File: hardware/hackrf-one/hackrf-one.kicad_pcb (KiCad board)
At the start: 4 copper layers, 120 x 75 mm, 431 parts, among them J1 USB-MICRO-B, J10 GND_CLIP, J2 RF-SHIELD-FRAME, J3 RF-SHIELD-COVER, J4 MOUNTING_HOLE, J5 MOUNTING_HOLE, J6 MOUNTING_HOLE, J7 MOUNTING_HOLE, J8 MOUNTING_HOLE, J9 MOUNTING_HOLE, P13 GPO1, P14 XCVR_CLKOUT, P15 INTR, P16 CLKIN, P17 GPO6, P18 OEB, P19 GPO3, P2 CLKOUT, P20 GPIO, P21 REF_IN, P22 I2S, P23 DBGEN, P24 TRST, P25 LPC_ISP, P26 LPC_JTAG, P27 MIXER_SDATA, P28 SD, P29 CPLD_JTAG, P3 GND, P30 BANK2_AUX, P31 MIXER_SCLK, P32 MIXER_ENX, P33 MIXER_RESETX, P34 MIX_BYPASS, P35 !MIX_BYPASS, P37 SCL, P38 SDA, P39 SSP1_SCK, P4 ANTENNA, P40 SSP1_COPI, P41 SSP1_CIPO, P43 RX, P44 HP, P45 LP, P46 TX_MIX_BP, P47 RX_MIX_BP, P48 TX_AMP, P49 RX_AMP, P5 LEDS, P50 AMP_BYPASS, P51 !TX_AMP_PWR, P52 !RX_AMP_PWR, P53 CS_XCVR, P54 CS_AD, P55 TXENABLE, P56 RXENABLE, P57 XTAL2, P58 GCK1, P59 GCK2, P6 GPO4, P60 SGPIO_CLK, P61 DA0, P62 DA7, P63 DD0, P64 DD9, P65 DA4, P66 DD5, P67 RSSI, P68 SPIFI_CS, P69 VREGMODE, P7 GPO2, P70 EN_1V8, P71 ID, P72 GP_CLKIN, P73 P1_2, P74 P1_1, P75 GP_CLKIN, P76 GP_CLKIN, P77 GP_CLKIN, P78 GP_CLKIN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

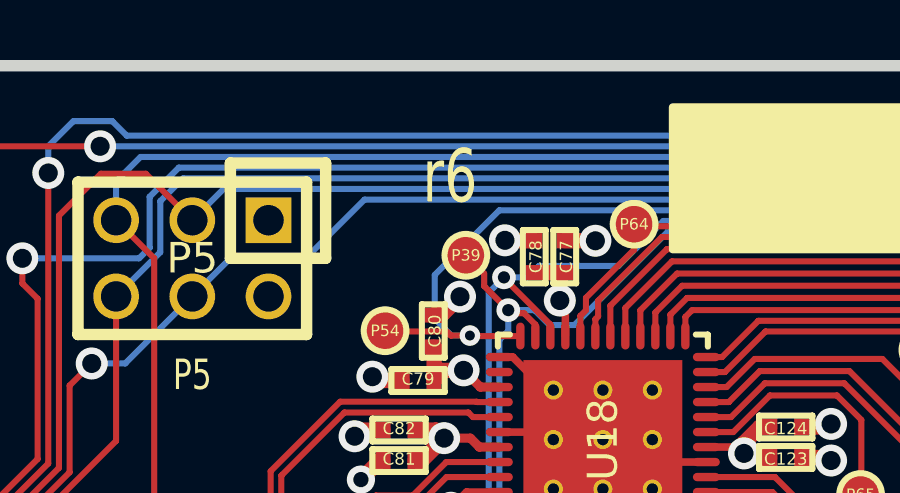
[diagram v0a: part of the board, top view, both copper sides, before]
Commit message: HackRF One: Change all references from r6 to r8
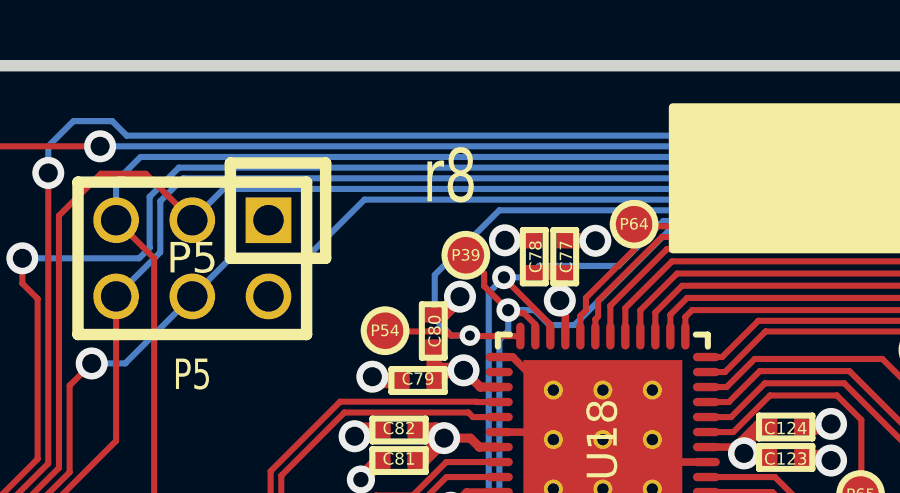
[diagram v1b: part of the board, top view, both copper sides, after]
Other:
- board text added: "r8"
- board text removed: "r6"
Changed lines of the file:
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@@
     (title "HackRF One")
     (date 2020-07-21)
-    (rev r6)
+    (rev r8)
     (company "Copyright 2012-2020 Great Scott Gadgets")
     (comment 1 "Michael Ossmann")
@@
       (net 192 GND))
   )
-  (gr_text r6 (at 97.8 103.7) (layer F.SilkS)
+  (gr_text r8 (at 97.8 103.7) (layer F.SilkS)
     (effects (font (size 1.778 1.27) (thickness 0.3048)))
   )

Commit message: HackRF One: update VBUS sense resistor values
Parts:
- R62: value 0 -> 10k
- R65: value 10k -> 18k
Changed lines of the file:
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@@
       (effects (font (size 0.4064 0.4064) (thickness 0.1016)))
     )
-    (fp_text value 0 (at 0 0.0508) (layer F.SilkS) hide
+    (fp_text value 10k (at 0 0.0508) (layer F.SilkS) hide
       (effects (font (size 0.4064 0.4064) (thickness 0.1016)))
     )
@@
       (effects (font (size 0.4064 0.4064) (thickness 0.1016)))
     )
-    (fp_text value 10k (at 0 0.0508 180) (layer F.SilkS) hide
+    (fp_text value 18k (at 0 0.0508 180) (layer F.SilkS) hide
       (effects (font (size 0.4064 0.4064) (thickness 0.1016)))
     )

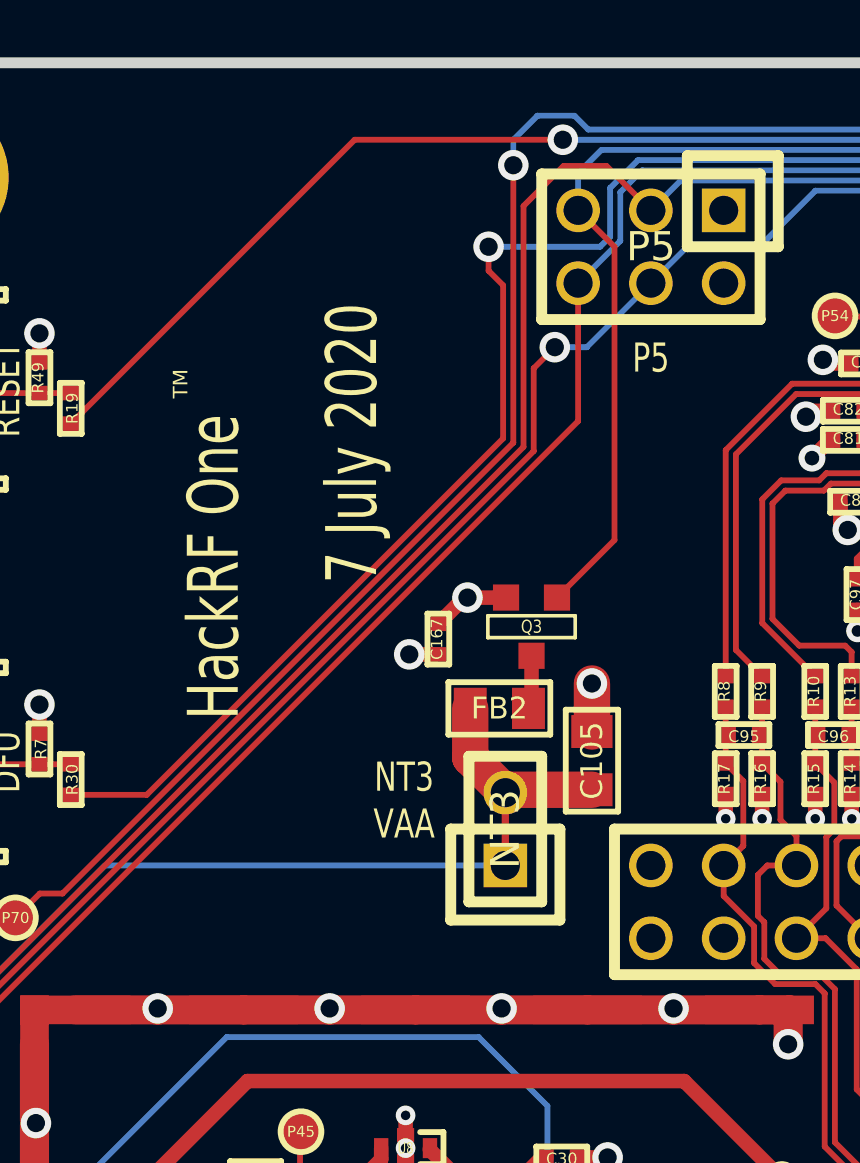
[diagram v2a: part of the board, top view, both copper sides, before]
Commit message: HackRF One: Update documentation
Update date codes
Move NT3 on silkscreen
Add VBUSCTRL note to .sch
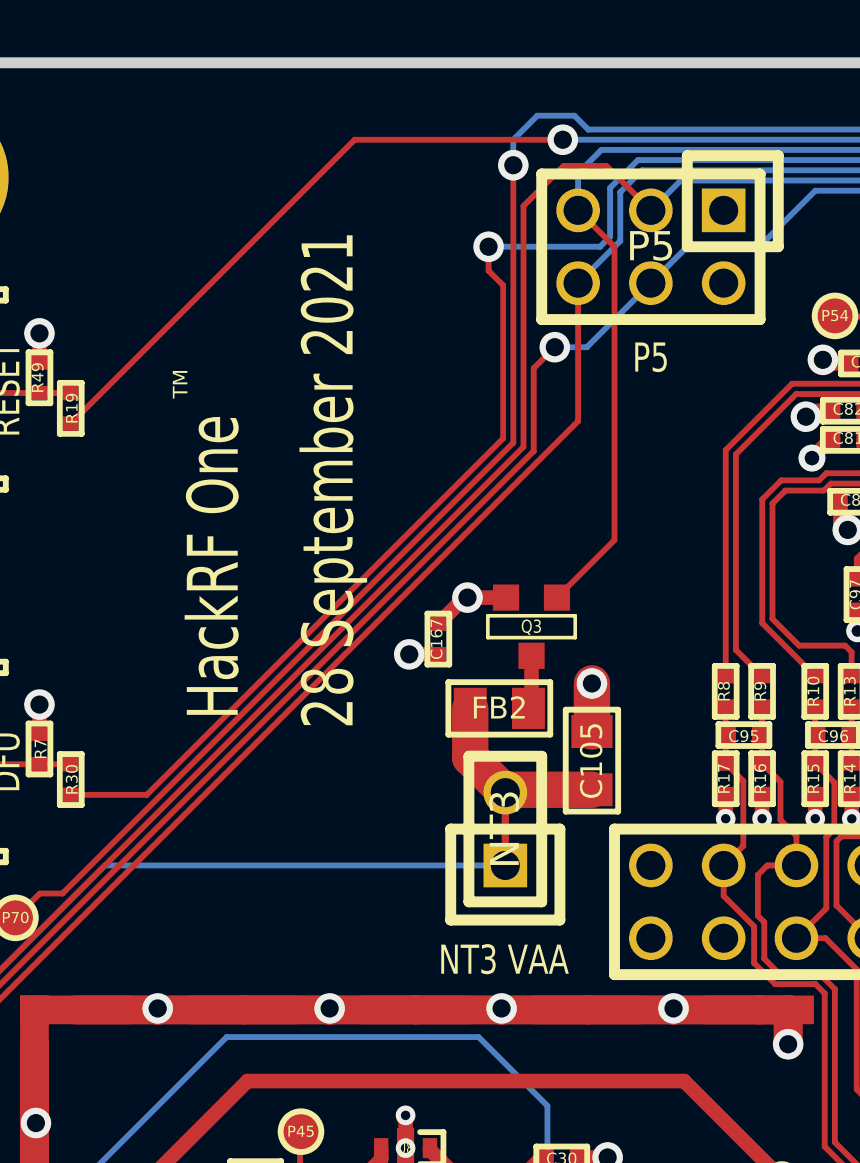
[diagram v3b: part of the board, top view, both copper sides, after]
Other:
- board text added: "28 September 2021"
- board text removed: "7 July 2020"
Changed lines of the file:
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@@
-(kicad_pcb (version 20171130) (host pcbnew 5.1.6)
+(kicad_pcb (version 20171130) (host pcbnew 5.1.5+dfsg1-2build2)
   (general
     (thickness 1.6002)
@@
   (title_block
     (title "HackRF One")
-    (date 2020-07-21)
+    (date 2021-09-28)
     (rev r8)
     (company "Copyright 2012-2020 Great Scott Gadgets")
@@
     (34 B.Paste user)
     (35 F.Paste user)
-    (36 B.SilkS user hide)
+    (36 B.SilkS user)
     (37 F.SilkS user)
-    (38 B.Mask user)
+    (38 B.Mask user hide)
     (39 F.Mask user hide)
     (41 Cmts.User user)
@@
     (effects (font (size 1.016 1.016) (thickness 0.1778)))
   )
-  (gr_text "7 July 2020" (at 78.796 113.278 90) (layer F.SilkS)
+  (gr_text "28 September 2021" (at 77.978 114.554 90) (layer F.SilkS)
     (effects (font (size 1.778 1.27) (thickness 0.3048)))
   )
@@
     (effects (font (size 1.016 0.762) (thickness 0.1905)))
   )
-  (gr_text "NT3\nVAA" (at 80.5994 125.7494) (layer F.SilkS)
+  (gr_text "NT3 VAA" (at 84.074 131.318) (layer F.SilkS)
     (effects (font (size 1.016 0.762) (thickness 0.1905)))
   )

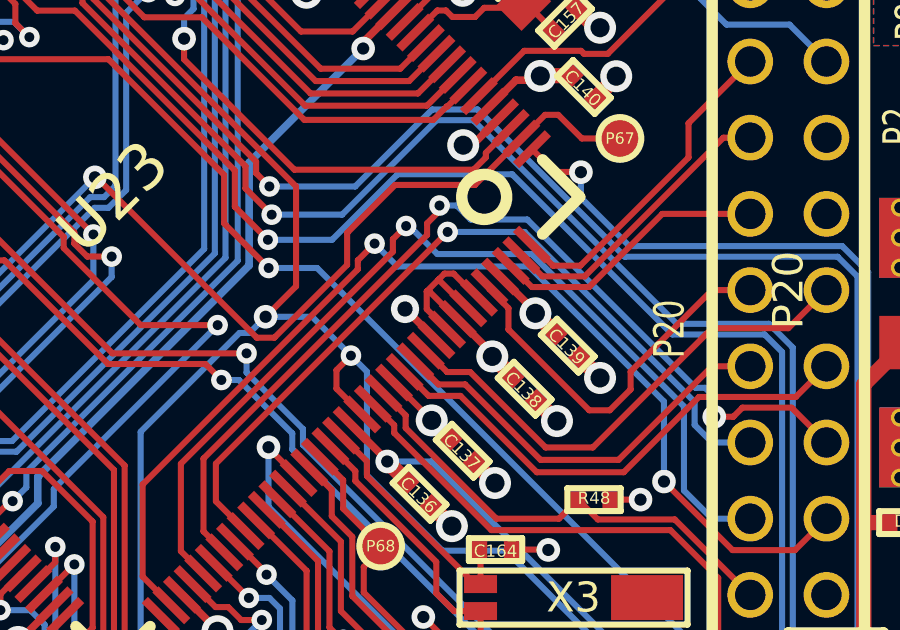
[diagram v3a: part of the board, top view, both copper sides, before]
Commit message: Adjust pin strapping to indicate revision increment.
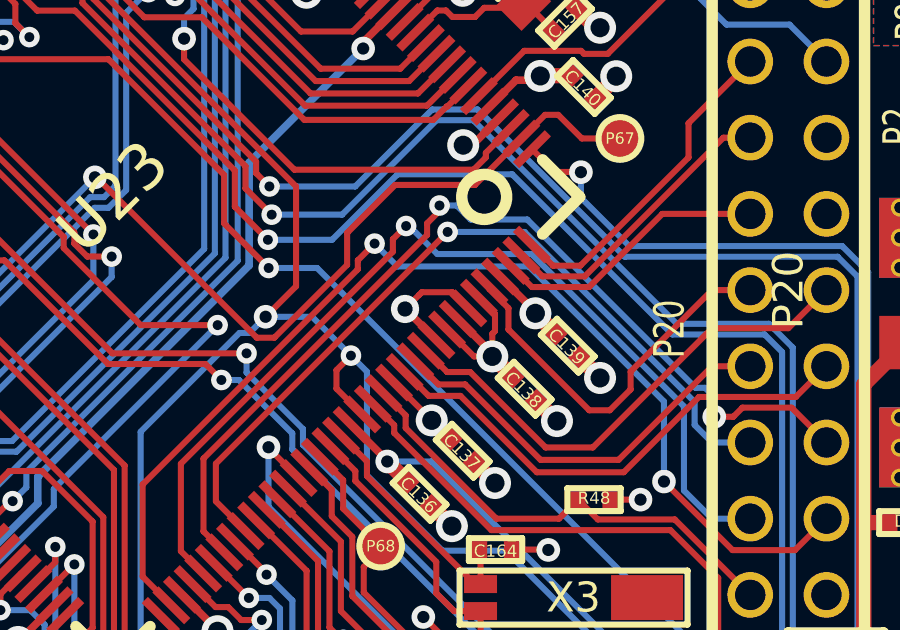
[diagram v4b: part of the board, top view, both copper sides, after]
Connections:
- P25 pad 3: (no net) -> Net-(P25-Pad3)
- P26 pad 7: (no net) -> Net-(P26-Pad7)
- U12 pad 2: (no net) -> Net-(U12-Pad2)
- U14 pad 2: (no net) -> Net-(U14-Pad2)
- U15 pad 4: (no net) -> Net-(U15-Pad4)
- U15 pad 6: (no net) -> Net-(U15-Pad6)
- U17 pad 12: (no net) -> Net-(U17-Pad12)
- U17 pad 14: (no net) -> Net-(U17-Pad14)
- U17 pad 18: (no net) -> Net-(U17-Pad18)
- U17 pad 3: (no net) -> Net-(U17-Pad3)
- U17 pad 33: (no net) -> Net-(U17-Pad33)
- U17 pad 34: (no net) -> Net-(U17-Pad34)
- U17 pad 40: (no net) -> Net-(U17-Pad40)
- U17 pad 6: (no net) -> Net-(U17-Pad6)
- U17 pad 8: (no net) -> Net-(U17-Pad8)
- U17 pad 9: (no net) -> Net-(U17-Pad9)
- U18 pad 38: (no net) -> Net-(U18-Pad38)
- U23 pad 138: VCC -> GND
- U23 pad 85: (no net) -> Net-(U23-Pad85)
- U23 pad 89: (no net) -> Net-(U23-Pad89)
- U23 pad 90: (no net) -> Net-(U23-Pad90)
- U24 pad 14: (no net) -> Net-(U24-Pad14)
- U24 pad 15: (no net) -> Net-(U24-Pad15)
- U24 pad 16: (no net) -> Net-(U24-Pad16)
- U24 pad 20: (no net) -> Net-(U24-Pad20)
- U24 pad 25: (no net) -> Net-(U24-Pad25)
- U24 pad 44: (no net) -> Net-(U24-Pad44)
- U24 pad 46: (no net) -> Net-(U24-Pad46)
- U24 pad 49: (no net) -> Net-(U24-Pad49)
- U24 pad 50: (no net) -> Net-(U24-Pad50)
- U24 pad 52: (no net) -> Net-(U24-Pad52)
- U24 pad 53: (no net) -> Net-(U24-Pad53)
- U24 pad 54: (no net) -> Net-(U24-Pad54)
- U24 pad 58: (no net) -> Net-(U24-Pad58)
- U24 pad 59: (no net) -> Net-(U24-Pad59)
- U24 pad 60: (no net) -> Net-(U24-Pad60)
- U24 pad 63: (no net) -> Net-(U24-Pad63)
- U24 pad 65: (no net) -> Net-(U24-Pad65)
- U24 pad 66: (no net) -> Net-(U24-Pad66)
- U24 pad 68: (no net) -> Net-(U24-Pad68)
- U24 pad 73: (no net) -> Net-(U24-Pad73)
- U24 pad 75: (no net) -> Net-(U24-Pad75)
- U24 pad 80: (no net) -> Net-(U24-Pad80)
- U24 pad 82: (no net) -> Net-(U24-Pad82)
- U24 pad 85: (no net) -> Net-(U24-Pad85)
- U24 pad 86: (no net) -> Net-(U24-Pad86)
- U24 pad 87: (no net) -> Net-(U24-Pad87)
- U24 pad 93: (no net) -> Net-(U24-Pad93)
- U24 pad 95: (no net) -> Net-(U24-Pad95)
- U24 pad 96: (no net) -> Net-(U24-Pad96)
- U4 pad 1: (no net) -> Net-(U4-Pad1)
- U4 pad 11: (no net) -> Net-(U4-Pad11)
- U4 pad 13: (no net) -> Net-(U4-Pad13)
- U4 pad 14: (no net) -> Net-(U4-Pad14)
- U4 pad 17: (no net) -> Net-(U4-Pad17)
- U4 pad 18: (no net) -> Net-(U4-Pad18)
- U4 pad 2: (no net) -> Net-(U4-Pad2)
- U4 pad 20: (no net) -> Net-(U4-Pad20)
- U4 pad 21: (no net) -> Net-(U4-Pad21)
- U4 pad 3: (no net) -> Net-(U4-Pad3)
- U9 pad 2: (no net) -> Net-(U9-Pad2)
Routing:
- net GND: track 592.3 -> 594.9 mm
- net VCC: track 187.8 -> 185.2 mm
